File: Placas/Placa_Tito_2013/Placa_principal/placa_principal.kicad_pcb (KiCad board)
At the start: 2 copper layers, 65 x 104 mm, 80 parts, among them IC1 ATMEGA88A-A, K1 Servo, P1 ADICIONAL 5V, P10 Batería 3,6V, P2 ADICIONAL GND, P3 ADICIONAL 5V, P4 ADICIONAL GND, P5 Puerto Serie, P6 Programador, P7 Motor 1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

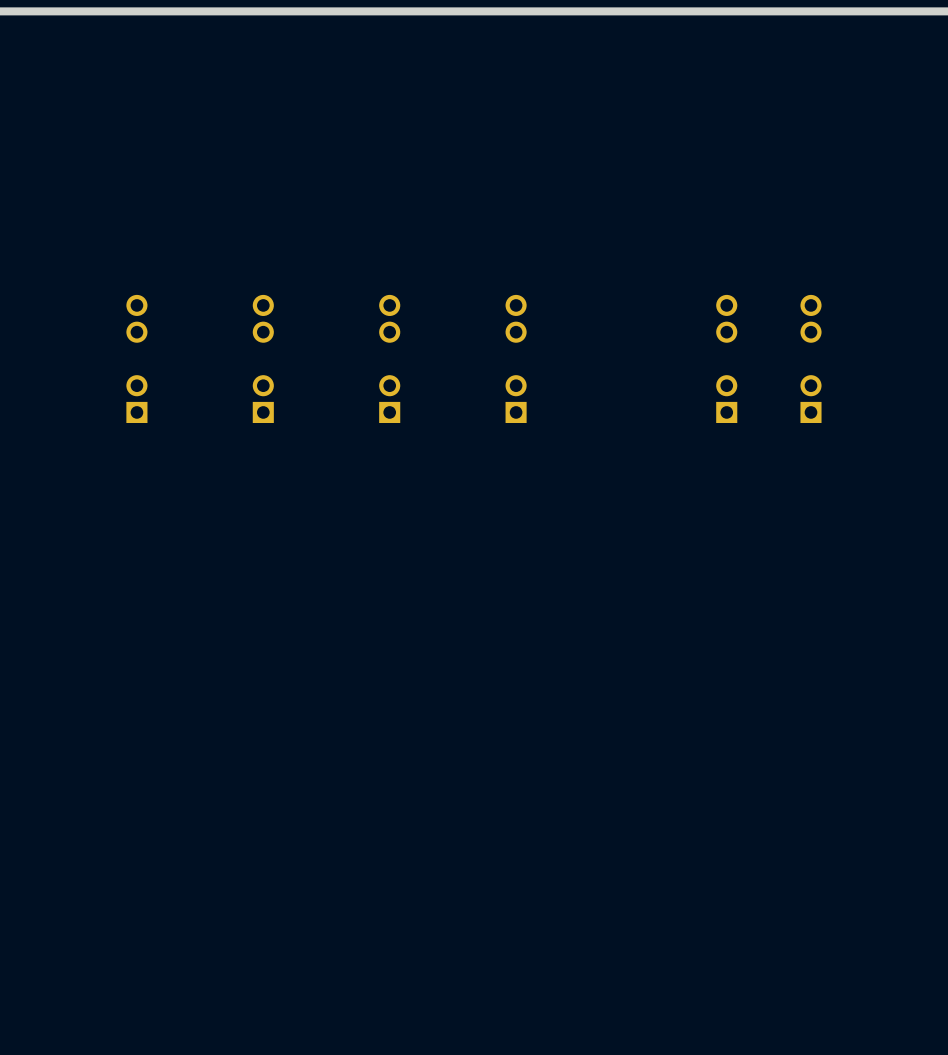
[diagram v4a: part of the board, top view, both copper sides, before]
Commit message: Preparado para hacer un tcrt1000 de patas dobladas
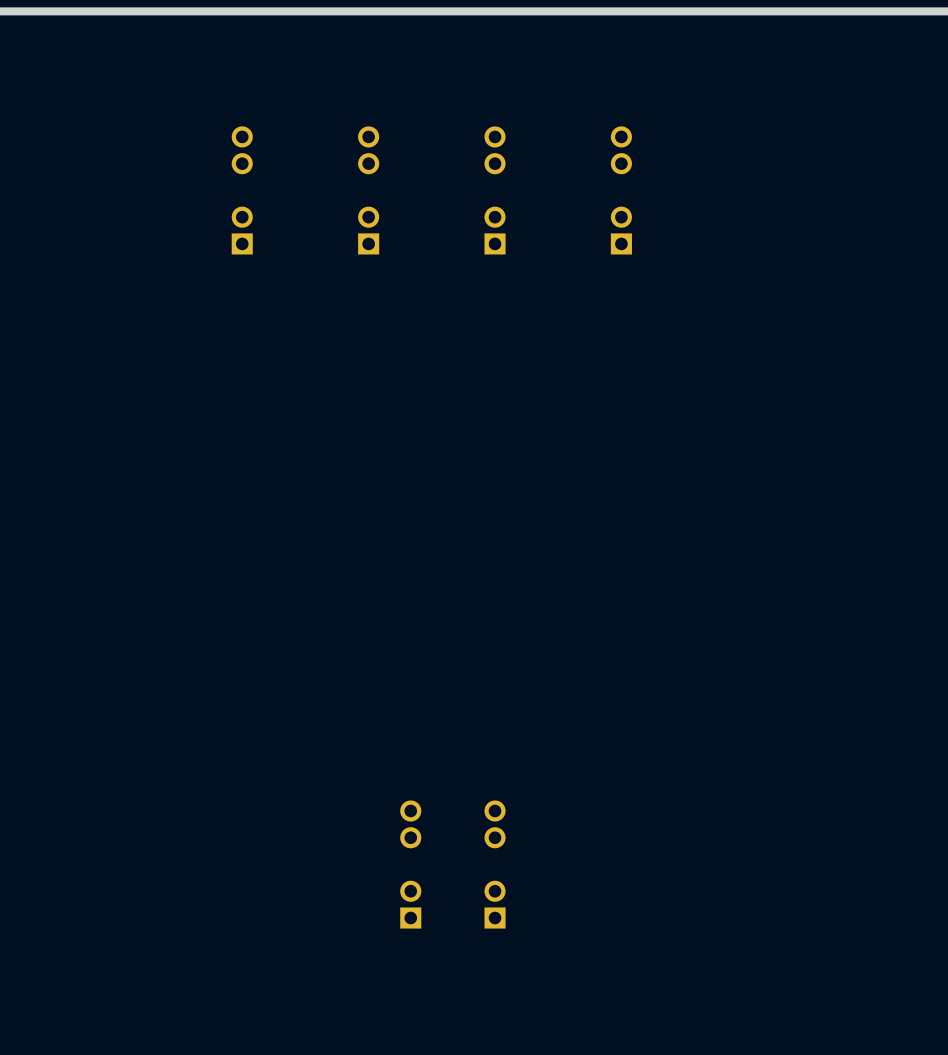
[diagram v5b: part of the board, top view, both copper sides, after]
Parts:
- moved U6 28.3 mm to (57.5, 93.5)
- moved U7 28.3 mm to (61.5, 93.5)
- moved U2 9.43 mm to (49.5, 61.5)
- moved U3 9.43 mm to (55.5, 61.5)
- moved U4 9.43 mm to (61.5, 61.5)
- moved U5 9.43 mm to (67.5, 61.5)
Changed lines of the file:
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@@
     (links 171)
     (no_connects 171)
-    (area 26.809499 53.409499 194.915288 182.1988)
+    (area 26.809499 52.809499 194.915288 182.1988)
     (thickness 1.6002)
     (drawings 4)
@@
   )
   (module TCRT1000 (layer Back)
-    (at 44.5 69.5 90)
+    (at 49.5 61.5 90)
     (fp_text reference U2 (at 0 2.25044 90) (layer B.SilkS)
       (effects (font (size 0.9525 0.9525) (thickness 0.23876)) (justify mirror))
@@
   )
   (module TCRT1000 (layer Back)
-    (at 62.5 69.5 90)
+    (at 67.5 61.5 90)
     (fp_text reference U5 (at 0 2.25044 90) (layer B.SilkS)
       (effects (font (size 0.9525 0.9525) (thickness 0.23876)) (justify mirror))
@@
   )
   (module TCRT1000 (layer Back)
-    (at 50.5 69.5 90)
+    (at 55.5 61.5 90)
     (fp_text reference U3 (at 0 2.25044 90) (layer B.SilkS)
       (effects (font (size 0.9525 0.9525) (thickness 0.23876)) (justify mirror))
@@
   )
   (module TCRT1000 (layer Back)
-    (at 72.5 69.5 90)
+    (at 57.5 93.5 90)
     (fp_text reference U6 (at 0 2.25044 90) (layer B.SilkS)
       (effects (font (size 0.9525 0.9525) (thickness 0.23876)) (justify mirror))
@@
   )
   (module TCRT1000 (layer Back)
-    (at 76.5 69.5 90)
+    (at 61.5 93.5 90)
     (fp_text reference U7 (at 0 2.25044 90) (layer B.SilkS)
       (effects (font (size 0.9525 0.9525) (thickness 0.23876)) (justify mirror))
@@
   )
   (module TCRT1000 (layer Back)
-    (at 56.5 69.5 90)
+    (at 61.5 61.5 90)
     (fp_text reference U4 (at 0 2.25044 90) (layer B.SilkS)
       (effects (font (size 0.9525 0.9525) (thickness 0.23876)) (justify mirror))

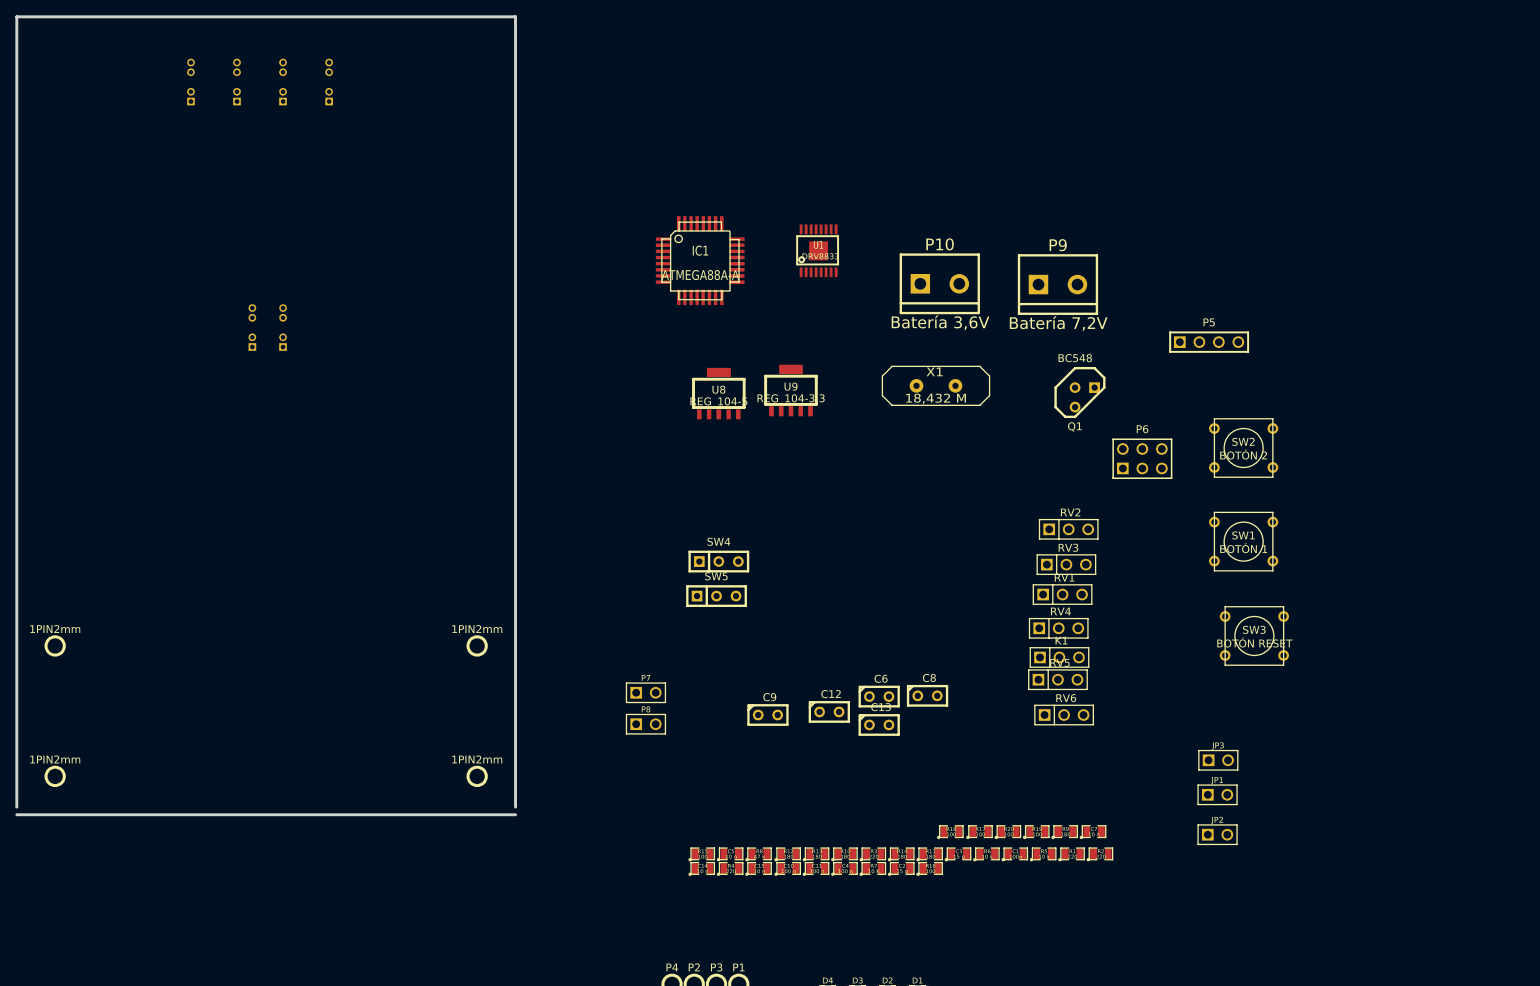
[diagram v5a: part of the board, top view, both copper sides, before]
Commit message: Colocados 8 sensores en la placa.
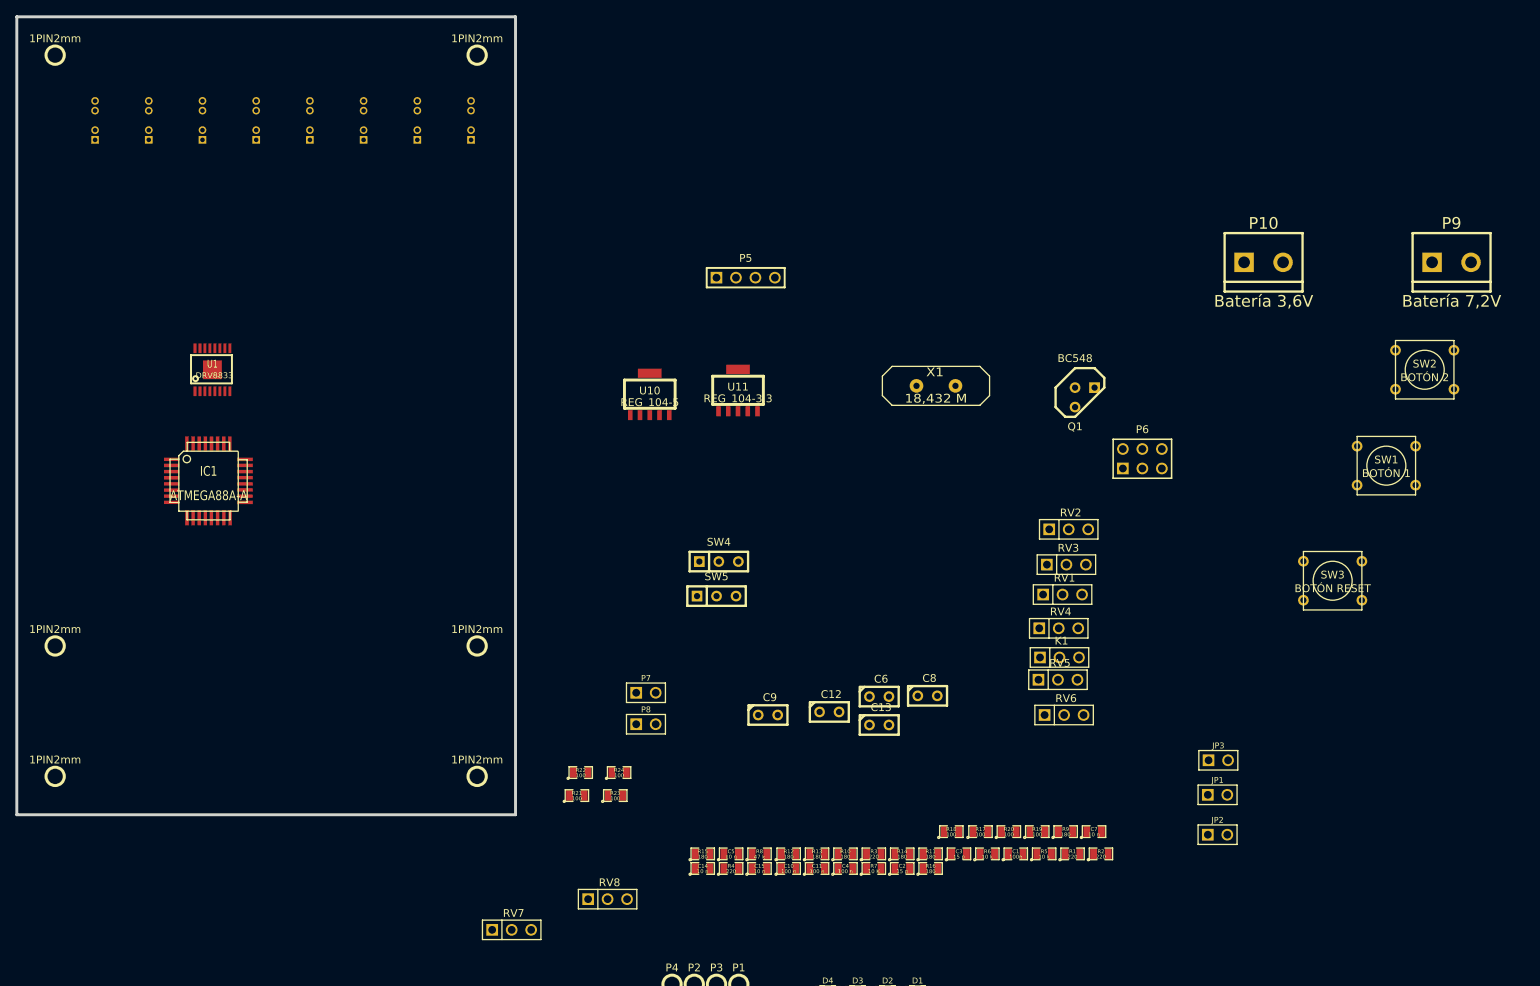
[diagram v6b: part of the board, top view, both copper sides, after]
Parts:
- added 1PIN2mm: P***, 1PIN2mm, F.Cu at (32.0, 58.0)
- added 1PIN2mm: P***, 1PIN2mm, F.Cu at (87.0, 58.0)
- added R21: 100, SM0805, F.Cu at (100.0, 154.5)
- added R22: 100, SM0805, F.Cu at (100.5, 151.5)
- added R23: 100, SM0805, F.Cu at (105.0, 154.5)
- added R24: 100, SM0805, F.Cu at (105.5, 151.5)
- added RV7: POT 20 k, PIN_ARRAY_3X1, F.Cu at (91.5, 172.0)
- added RV8: POT 20 k, PIN_ARRAY_3X1, F.Cu at (104.0, 168.0)
- added U10: REG_104-5, SOT223-5, F.Cu at (109.5, 102.5)
- added U11: REG_104-3.3, SOT223-5, F.Cu at (121.0, 102.0)
- R15, R16: value 100 -> 180
- U8: value REG_104-5 -> TCRT1000; footprint SOT223-5 -> TCRT1000; moved to B.Cu
- U9: value REG_104-3.3 -> TCRT1000; footprint SOT223-5 -> TCRT1000; moved to B.Cu
- moved U1 80.5 mm to (52.5, 99.0)
- moved IC1 70.2 mm to (52.0, 113.5)
- moved P5 61.0 mm to (122.0, 87.0)
- moved U9 54.9 mm to (86.0, 66.5), turned to 90 degrees
- moved U8 53.4 mm to (79.0, 66.5), turned to 90 degrees
- moved P9 51.4 mm to (214.0, 85.0)
- moved P10 42.3 mm to (189.5, 85.0)
- moved U7 29.0 mm to (72.0, 66.5)
- moved U6 28.0 mm to (65.0, 66.5)
- moved SW2 25.7 mm to (210.5, 99.0)
- moved SW1 21.1 mm to (205.5, 111.5)
- moved U2 13.5 mm to (37.0, 66.5)
- moved U3 12.5 mm to (44.0, 66.5)
- moved SW3 12.5 mm to (198.5, 126.5)
- moved U4 11.6 mm to (51.0, 66.5)
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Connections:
- IC1 pad 19: (no net) -> /Sensores/Sensor 7
- IC1 pad 22: (no net) -> /Sensores/Sensor 8
- R15 pad 1: N-0000062 -> N-0000053
- R15 pad 2: GND -> /Sensores/Habilitador sensores
- R16 pad 1: N-0000063 -> N-0000064
- R16 pad 2: GND -> /Sensores/Habilitador sensores
- R17 pad 1: N-0000061 -> N-0000056
- R18 pad 1: N-0000064 -> N-0000057
- R20 pad 1: N-0000059 (its old number) -> N-0000068
- RV1 pad 1: N-0000062 -> N-0000056
- RV2 pad 1: N-0000063 -> N-0000057
- RV3 pad 1: N-0000061 -> N-0000058
- RV4 pad 1: N-0000064 -> N-0000068
- RV5 pad 1: N-0000058 -> N-0000061
- RV6 pad 1: N-0000059 (its old number) -> N-0000055
- U8 pad 1: N-0000039 -> N-0000053
- U8 pad 2: +5V -> GND
- U8 pad 3: GND -> /Sensores/Sensor 7
- U8 pad 4: N-0000040 -> +5V
- U9 pad 1: N-0000037 -> N-0000064
- U9 pad 2: +3.3V -> GND
- U9 pad 3: GND -> /Sensores/Sensor 8
- U9 pad 4: N-0000041 -> +5V
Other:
- outline, holes or cut-outs redrawn

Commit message: Empezados a colocar componentes en la placa
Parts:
- added 1PIN2mm: P***, 1PIN2mm, F.Cu at (59.5, 75.5)
- IC1, U1, U10, U11: moved to B.Cu
- SW5: value INTERRUPTOR BATERÍA 3,7V -> INTERRUPTOR REGULADOR 3,3V
- moved SW2 177.7 mm to (33.0, 90.0), turned to 270 degrees
- moved SW1 172.9 mm to (33.0, 100.0), turned to 270 degrees
- moved SW3 166.2 mm to (33.0, 111.0), turned to 270 degrees
- moved RV3 145.8 mm to (51.0, 32.0), turned to 90 degrees
- moved RV6 144.3 mm to (72.8, 31.8), turned to 90 degrees
- moved RV1 143.4 mm to (57.0, 31.9), turned to 90 degrees
- moved K1 142.8 mm to (65.2, 32.4), turned to 90 degrees
- moved RV5 142.7 mm to (68.2, 32.5), turned to 90 degrees
- moved RV4 142.6 mm to (61.5, 32.5), turned to 90 degrees
- moved RV7 140.7 mm to (77.0, 32.0), turned to 90 degrees
- moved RV8 136.3 mm to (85.5, 33.0), turned to 90 degrees
- moved P1 131.5 mm to (38.1, 77.1)
- moved P2 131.5 mm to (32.3, 77.1)
- moved P3 131.5 mm to (35.2, 77.1)
- moved P4 131.5 mm to (29.4, 77.1)
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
